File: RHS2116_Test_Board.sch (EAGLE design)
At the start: 21 parts, among them J1 GRPB041VWVN-RC, J2 GRPB031VWVN-RC, U1 RHS2116_QFN, U2 TPS71921-22DRVT, U3 MSP430F2132_RHB_32

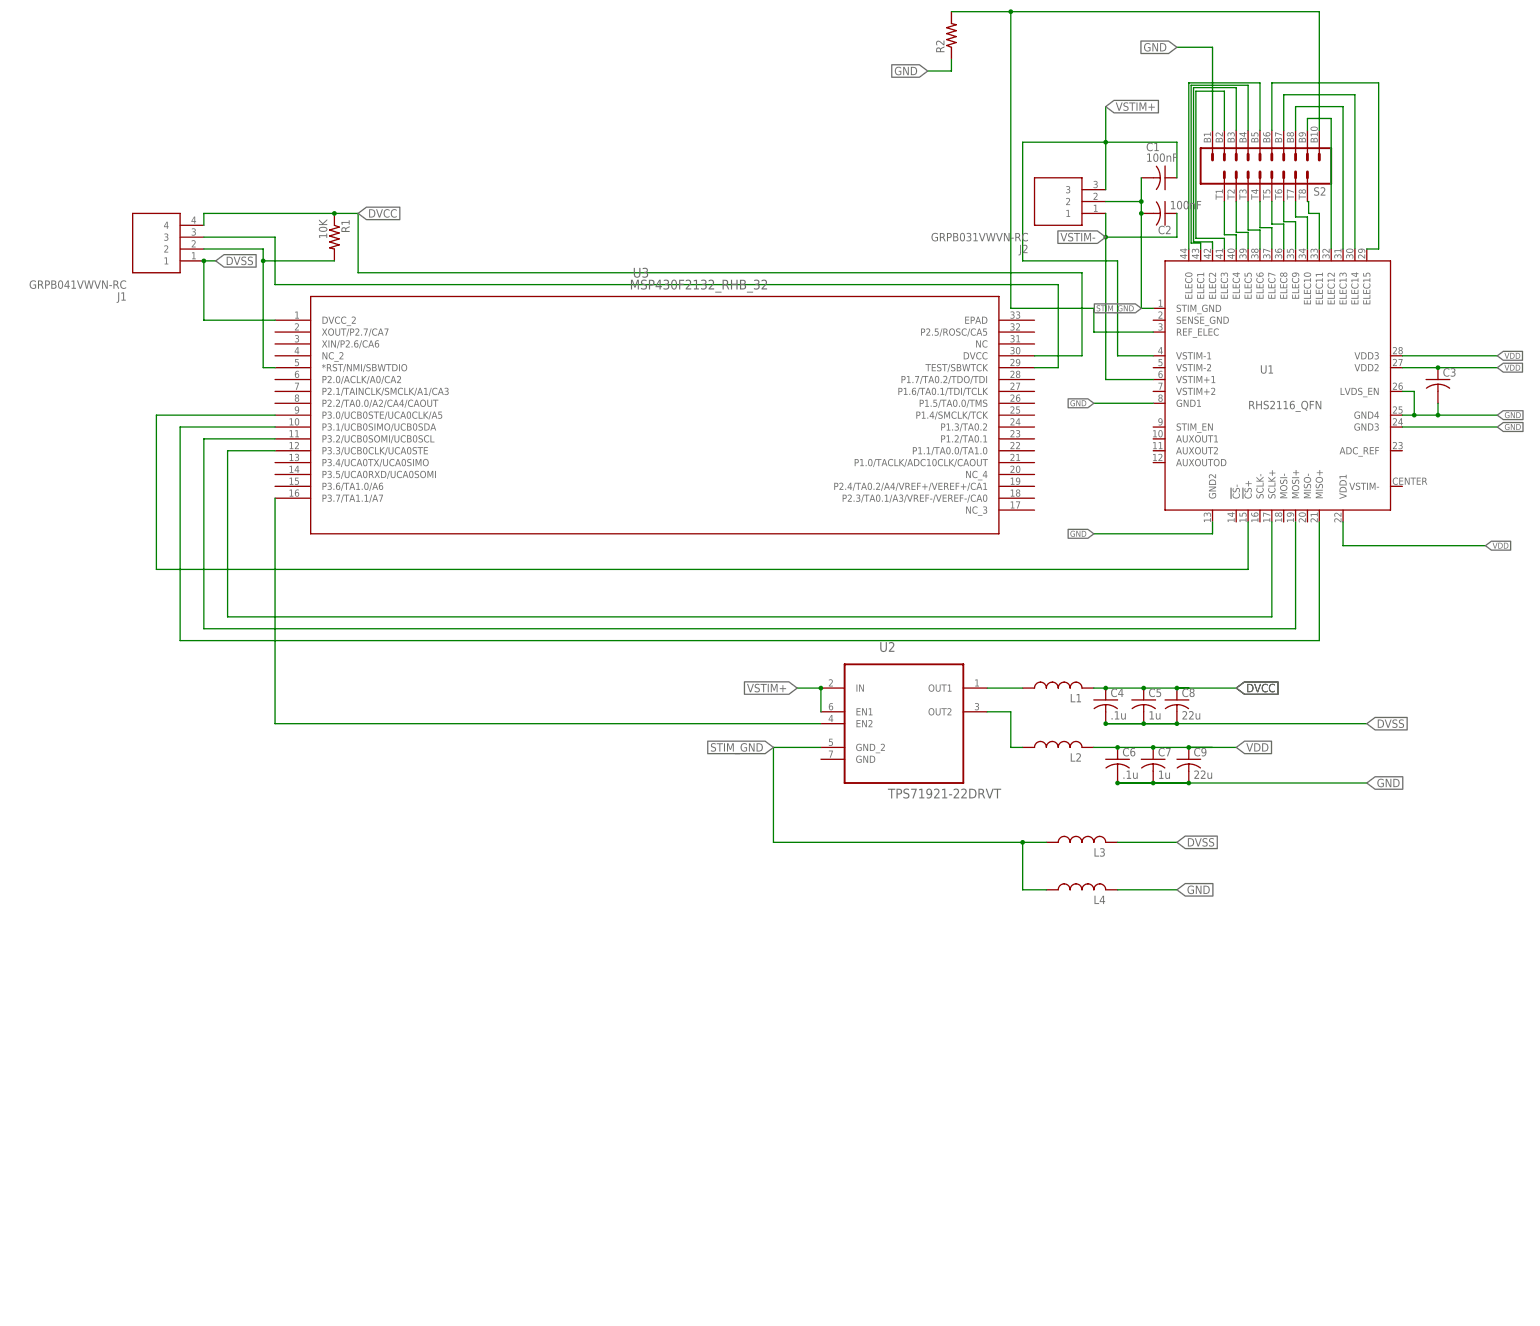
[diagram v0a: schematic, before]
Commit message: Added BGX13P schematic and footprint Added LM27762 schematic and footprint
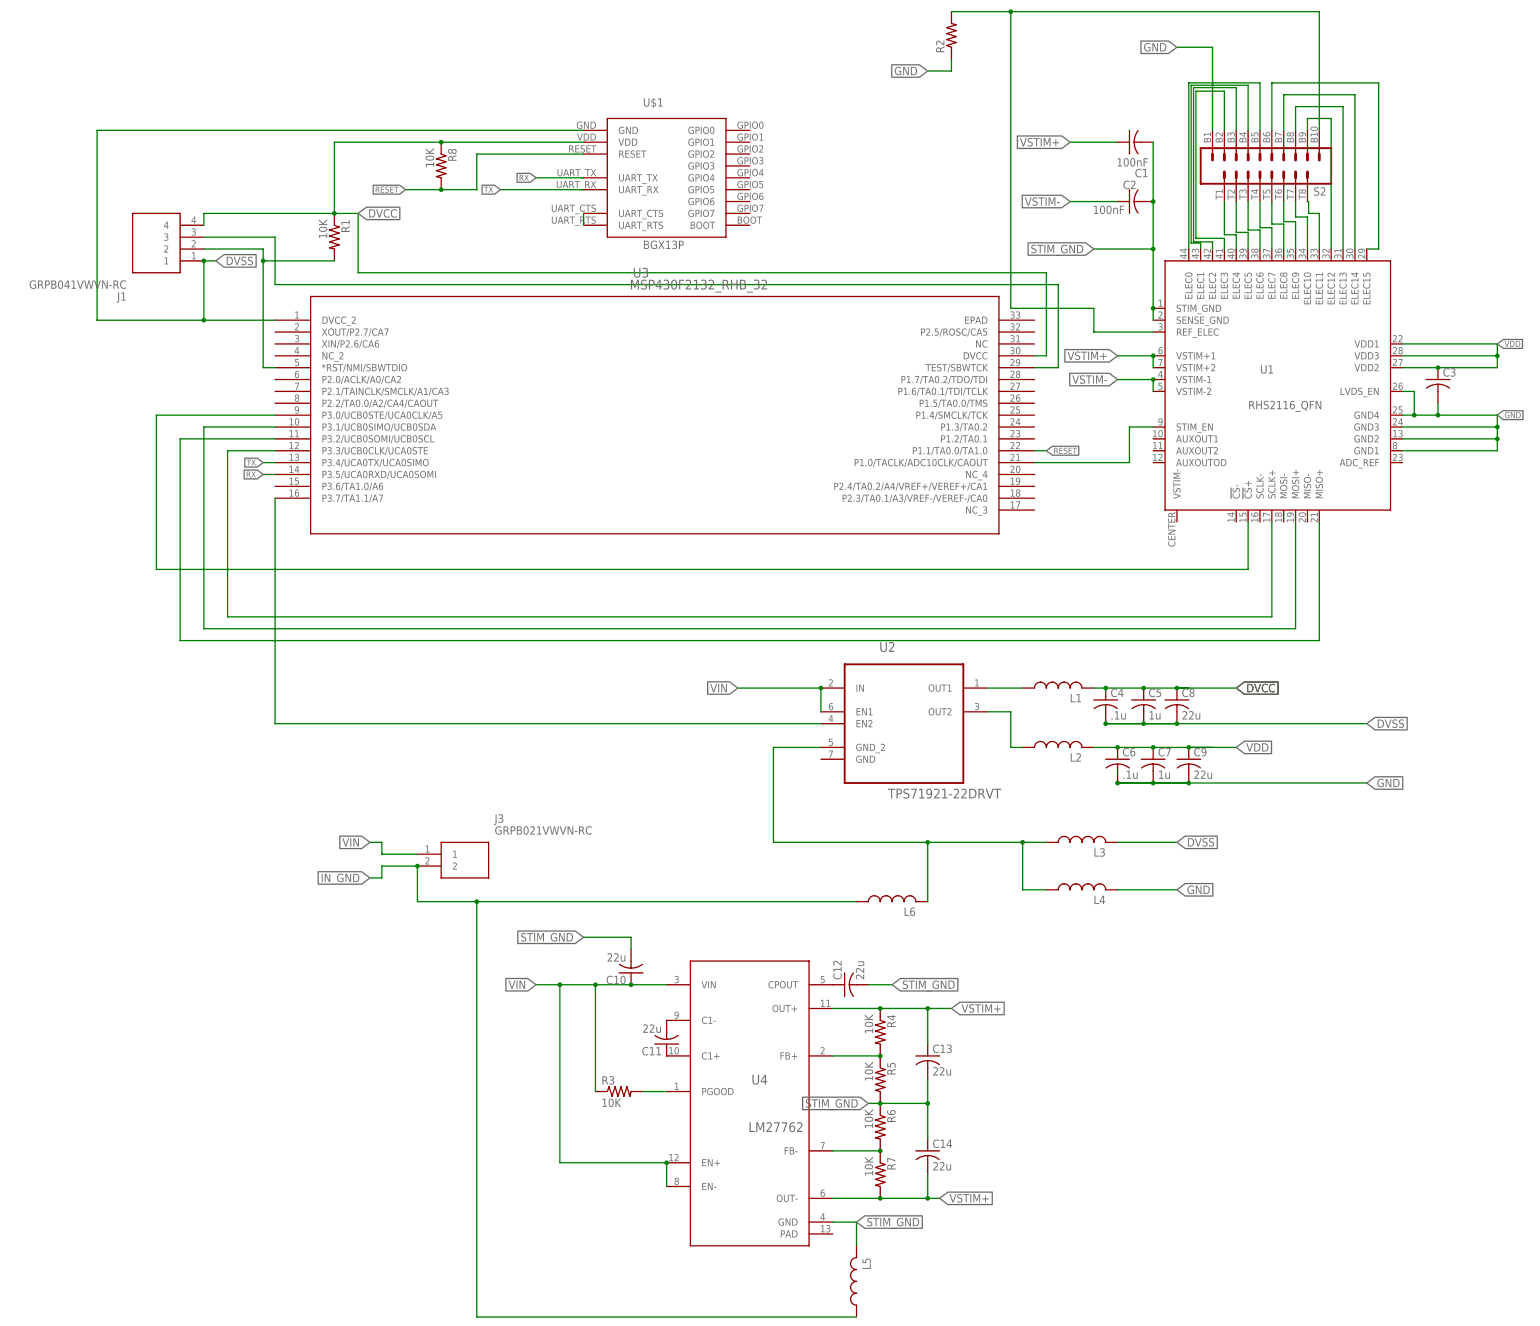
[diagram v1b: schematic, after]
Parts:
- removed J2: GRPB031VWVN-RC, GRPB031VWVN-RC:GRPB031VWVN-RC
- added C10, C11, C12, C13, C14: 22u, rcl:C-USC0805
- added J3: GRPB021VWVN-RC, GRPB021VWVN-RC:GRPB021VWVN-RC
- added L5, L6: (no value), rcl:L-USL0805
- added R3, R4, R5, R6, R7, R8: 10K, resistor:R-US_R0402
- added U$1: BGX13P, BGX13P:BGX13P
- added U4: LM27762, Texas Instruments_By_element14_Batch_1:LM27762DSSR
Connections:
- new net IN_GND: J3.2, L5.1, L6.1
- new net N$27: R3.2, U4.PGOOD
- new net N$28: C11.2, U4.C1-
- new net N$29: C11.1, U4.C1+
- new net N$30: C12.1, U4.CPOUT
- new net N$32: R4.2, R5.1, U4.FB+
- new net N$33: R6.2, R7.1, U4.FB-
- new net N$34: U$1.UART_CTS, U$1.UART_RTS
- new net N$5: U1.STIM_EN, U3.P1.0/TACLK/ADC10CLK/CAOUT
- new net RESET: R8.2, U$1.RESET, U3.P1.1/TA0.0/TA1.0
- new net RX: U$1.UART_TX, U3.P3.5/UCA0RXD/UCA0SOMI
- new net TX: U$1.UART_RX, U3.P3.4/UCA0TX/UCA0SIMO
- new net VIN: C10.1, J3.1, R3.1, U2.EN1, U2.IN, U4.EN+, U4.EN-, U4.VIN
- net DVCC: now also R8.1, U$1.VDD
- net DVSS: now also U$1.GND
- net N$2: now also U3.P3.1/UCB0SIMO/UCB0SDA; no longer U3.P3.2/UCB0SOMI/UCB0SCL
- net N$3: now also U3.P3.2/UCB0SOMI/UCB0SCL; no longer U3.P3.1/UCB0SIMO/UCB0SDA
- net STIM_GND: now also C10.2, C12.2, C13.2, C14.1, L5.2, L6.2, R5.2, R6.1, U1.SENSE_GND, U4.GND; no longer J2.2
- net VSTIM+: now also C13.1, C14.2, R4.1, R7.2, U1.VSTIM+1, U1.VSTIM+2, U4.OUT+, U4.OUT-; no longer J2.3, U1.VSTIM-1, U2.EN1, U2.IN
- net VSTIM-: now also U1.VSTIM-1, U1.VSTIM-2; no longer J2.1, U1.VSTIM+1
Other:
- moved on the sheet: C1, C2, U1

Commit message: Small schematic changes
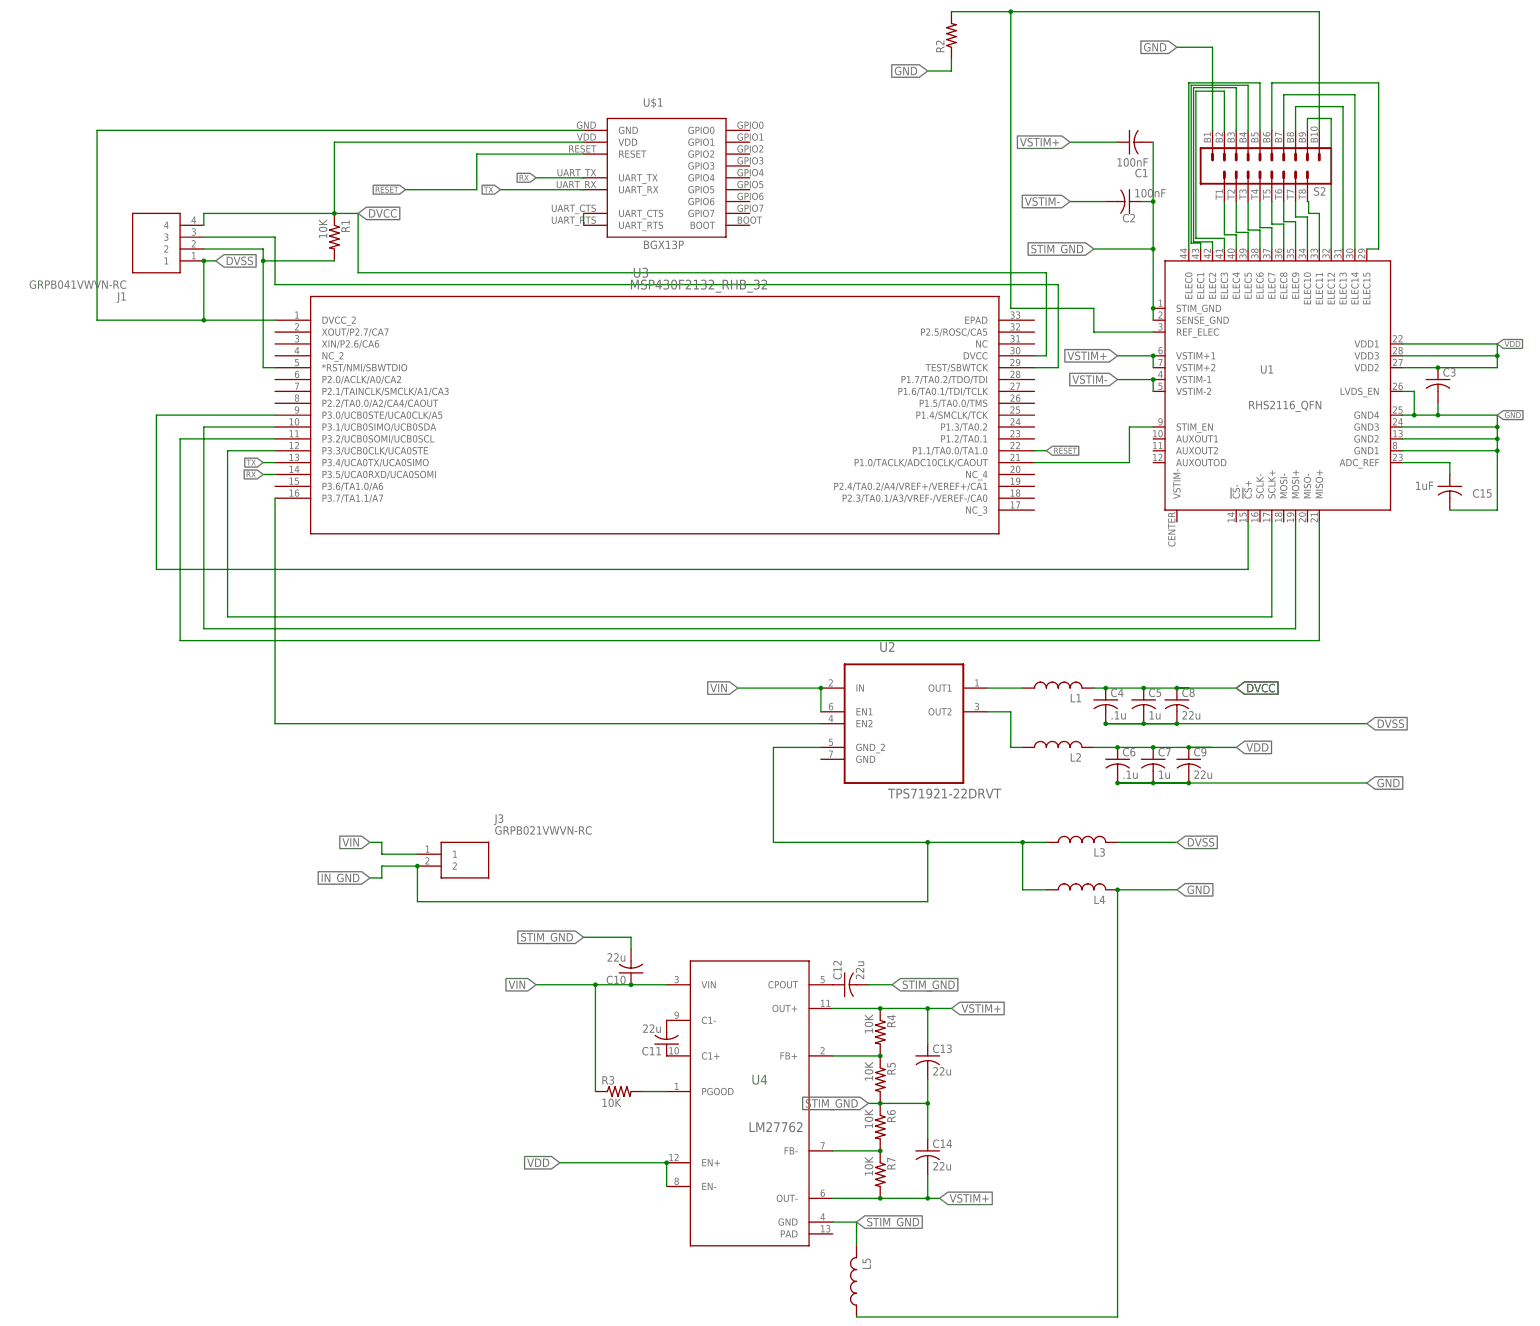
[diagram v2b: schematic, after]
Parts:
- removed L6: (no value), rcl:L-USL0805
- removed R8: 10K, resistor:R-US_R0402
- added C15: 1uF, resistor:C-USC0402
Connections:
- new net N$31: C15.1, U1.ADC_REF
- net DVCC: no longer R8.1
- net GND: now also C15.2, L5.1
- net IN_GND: now also L3.1, L4.1, U2.GND_2; no longer L5.1, L6.1
- net RESET: no longer R8.2
- net STIM_GND: now also C2.1; no longer C2.2, L3.1, L4.1, L6.2, U2.GND_2
- net VDD: now also U4.EN+, U4.EN-
- net VIN: no longer U4.EN+, U4.EN-
- net VSTIM-: now also C2.2; no longer C2.1
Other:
- moved on the sheet: C2
